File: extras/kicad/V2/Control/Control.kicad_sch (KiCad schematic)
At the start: 50 parts, among them J1 Ultrasonic Ranging, J2 Conn_01x05, J3 Output, J4 Input, J6 left, J7 right, P8 BeagleBone_Black_Header, P9 BeagleBone_Black_Header, U1 SparkFun-micromod, U2 ESP-01-WIFI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

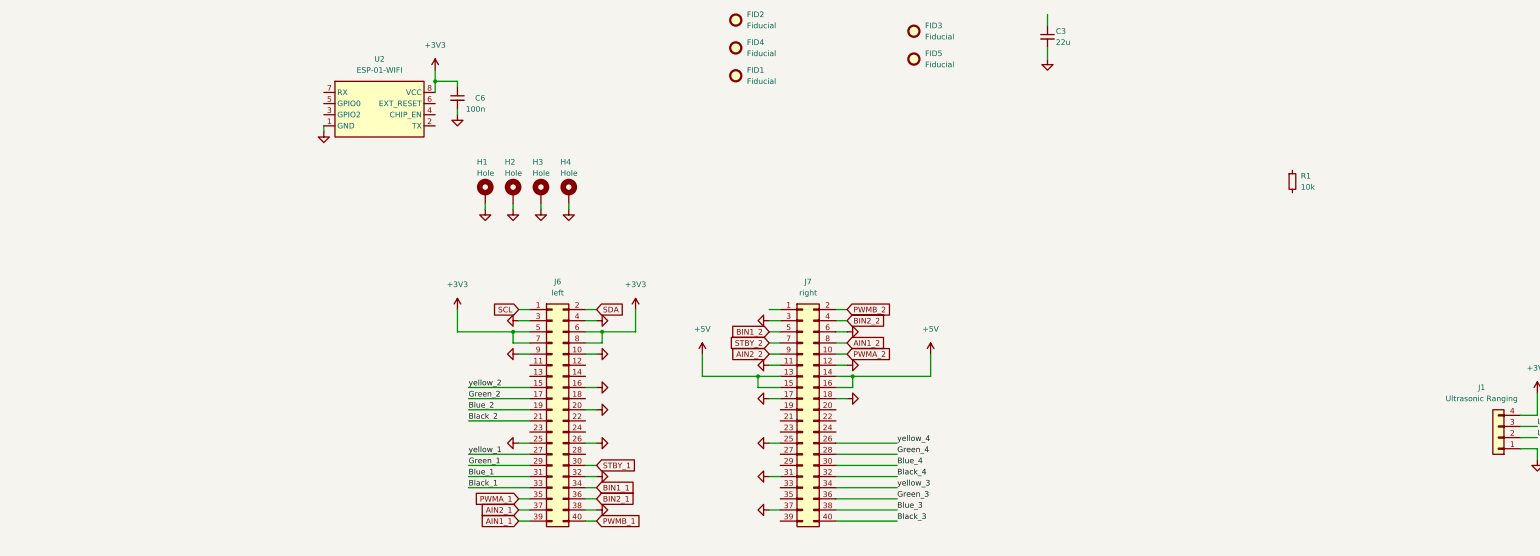
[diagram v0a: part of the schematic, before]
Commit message: Added UEXT, Mikroe & 7Pin SPI
(7pin SPI is break out garden) so we don't forget them
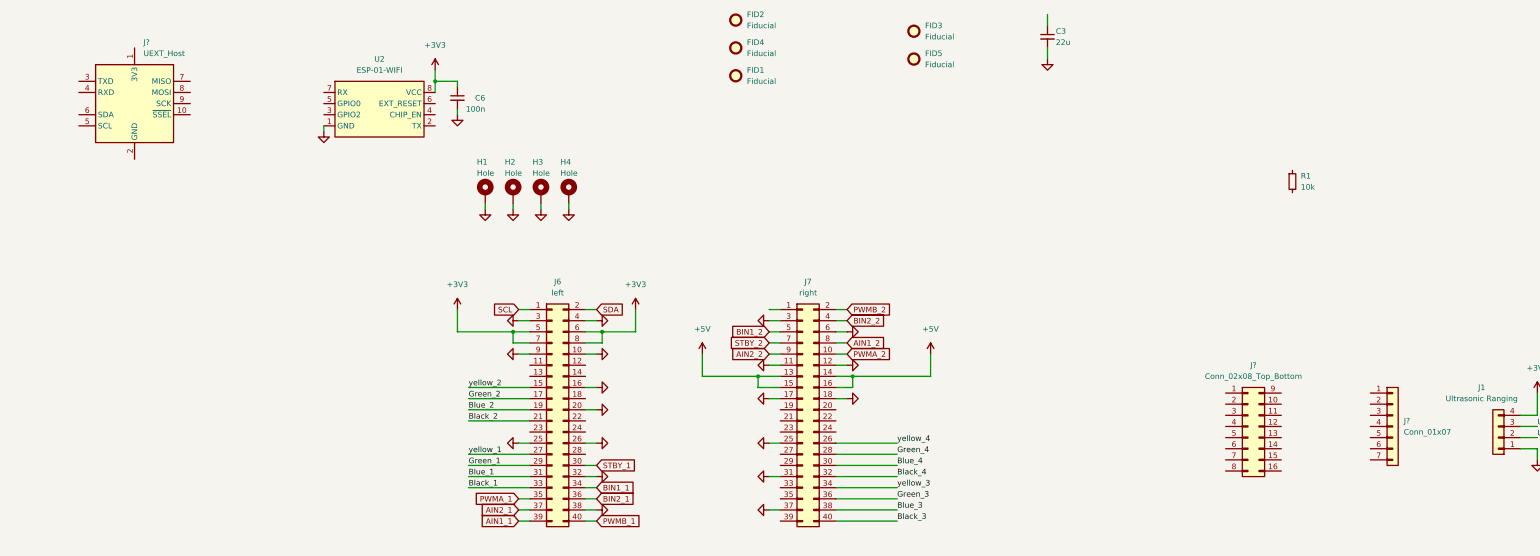
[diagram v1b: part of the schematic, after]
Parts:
- added J?: UEXT_Host, symbol Connector:UEXT_Host
- added J?: Conn_01x07, symbol Connector_Generic:Conn_01x07
- added J?: Conn_02x08_Top_Bottom, symbol Connector_Generic:Conn_02x08_Top_Bottom

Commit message: Added links to parts
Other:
- note added: "https://shop.pimoroni.com/products/spi-breakout-garden-extender-kit"
- note added: "https://www.mikroe.com/mikrobus-shuttle-127mm-2x8-pin-box-header-smd-male"
- note added: "https://www.olimex.com/Products/Modules/"
- moved on the sheet: J?
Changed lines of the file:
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@@
     (stroke (width 0) (type default) (color 0 0 0 0))
+  )
+  (text "https://shop.pimoroni.com/products/spi-breakout-garden-extender-kit"
+    (at 386.08 58.42 0)
+    (effects (font (size 1.27 1.27)) (justify left bottom))
   )
   (text "I2C ardress:\n001100X" (at 648.335 144.78 0)
@@
   )
   (text "0011[A2][A1][A0]" (at 536.575 146.685 0)
+    (effects (font (size 1.27 1.27)) (justify left bottom))
+  )
+  (text "https://www.mikroe.com/mikrobus-shuttle-127mm-2x8-pin-box-header-smd-male"
+    (at 368.3 35.56 0)
+    (effects (font (size 1.27 1.27)) (justify left bottom))
+  )
+  (text "https://www.olimex.com/Products/Modules/" (at 408.94 88.9 0)
     (effects (font (size 1.27 1.27)) (justify left bottom))
   )
@@
     (pin "1")
   )
-  (symbol (lib_id "Connector:UEXT_Host") (at 86.36 50.8 0) (unit 1)
-    (in_bom yes) (on_board yes) (fields_autoplaced)
-    (property "Reference" "J?" (id 0) (at 88.3794 36.83 0)
-      (effects (font (size 1.27 1.27)) (justify left))
-    )
-    (property "Value" "UEXT_Host" (id 1) (at 88.3794 39.37 0)
-      (effects (font (size 1.27 1.27)) (justify left))
-    )
-    (property "Footprint" "" (id 2) (at 82.55 50.8 0)
-      (effects (font (size 1.27 1.27)) hide)
-    )
-    (property "Datasheet" "https://www.olimex.com/Products/Modules/UEXT/resources/UEXT_rev_B.pdf" (id 3) (at 82.55 50.8 0)
+  (symbol (lib_id "Connector:UEXT_Host") (at 396.24 83.82 0) (unit 1)
+    (in_bom yes) (on_board yes) (fields_autoplaced)
+    (property "Reference" "J?" (id 0) (at 398.2594 69.85 0)
+      (effects (font (size 1.27 1.27)) (justify left))
+    )
+    (property "Value" "UEXT_Host" (id 1) (at 398.2594 72.39 0)
+      (effects (font (size 1.27 1.27)) (justify left))
+    )
+    (property "Footprint" "" (id 2) (at 392.43 83.82 0)
+      (effects (font (size 1.27 1.27)) hide)
+    )
+    (property "Datasheet" "https://www.olimex.com/Products/Modules/UEXT/resources/UEXT_rev_B.pdf" (id 3) (at 392.43 83.82 0)
       (effects (font (size 1.27 1.27)) hide)
     )
@@
     (pin "9")
   )
-  (symbol (lib_id "Connector_Generic:Conn_01x07") (at 373.38 124.46 0) (unit 1)
-    (in_bom yes) (on_board yes) (fields_autoplaced)
-    (property "Reference" "J?" (id 0) (at 375.92 123.1899 0)
-      (effects (font (size 1.27 1.27)) (justify left))
-    )
-    (property "Value" "Conn_01x07" (id 1) (at 375.92 125.7299 0)
-      (effects (font (size 1.27 1.27)) (justify left))
-    )
-    (property "Footprint" "" (id 2) (at 373.38 124.46 0)
-      (effects (font (size 1.27 1.27)) hide)
-    )
-    (property "Datasheet" "~" (id 3) (at 373.38 124.46 0)
+  (symbol (lib_id "Connector_Generic:Conn_01x07") (at 378.46 53.34 0) (unit 1)
+    (in_bom yes) (on_board yes) (fields_autoplaced)
+    (property "Reference" "J?" (id 0) (at 381 52.0699 0)
+      (effects (font (size 1.27 1.27)) (justify left))
+    )
+    (property "Value" "Conn_01x07" (id 1) (at 381 54.6099 0)
+      (effects (font (size 1.27 1.27)) (justify left))
+    )
+    (property "Footprint" "" (id 2) (at 378.46 53.34 0)
+      (effects (font (size 1.27 1.27)) hide)
+    )
+    (property "Datasheet" "~" (id 3) (at 378.46 53.34 0)
       (effects (font (size 1.27 1.27)) hide)
     )
@@
     (pin "1")
   )
-  (symbol (lib_id "Connector_Generic:Conn_02x08_Top_Bottom") (at 340.36 124.46 0) (unit 1)
-    (in_bom yes) (on_board yes) (fields_autoplaced)
-    (property "Reference" "J?" (id 0) (at 341.63 110.49 0))
-    (property "Value" "Conn_02x08_Top_Bottom" (id 1) (at 341.63 113.03 0))
-    (property "Footprint" "" (id 2) (at 340.36 124.46 0)
-      (effects (font (size 1.27 1.27)) hide)
-    )
-    (property "Datasheet" "~" (id 3) (at 340.36 124.46 0)
-      (effects (font (size 1.27 1.27)) hide)
-    )
+  (symbol (lib_id "Connector_Generic:Conn_02x08_Top_Bottom") (at 358.14 27.94 0) (unit 1)
+    (in_bom yes) (on_board yes) (fields_autoplaced)
+    (property "Reference" "J?" (id 0) (at 359.41 13.97 0))
+    (property "Value" "Conn_02x08_Top_Bottom" (id 1) (at 359.41 16.51 0))
+    (property "Footprint" "" (id 2) (at 358.14 27.94 0)
+      (effects (font (size 1.27 1.27)) hide)
+    )
+    (property "Datasheet" "~" (id 3) (at 358.14 27.94 0)
+      (effects (font (size 1.27 1.27)) hide)
+    )

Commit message: Update Control.kicad_sch
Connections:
- net +3V3: no longer U1.59 (SPI_COPI_(MOSI)), U1.61 (SPI_CIPO_(MISO)), U1.63 (G10), U1.65 (G9), U1.67 (G8), U1.69 (G7/BUS7), U1.71 (G6/BUS6), U1.73 (G5/BUS5)
- net BIN1_1: now also U1.66 (SDI_DATA1); no longer U1.51 (I2C_SDA1)
- net BIN2_1: now also U1.68 (SDI_DATA2); no longer U1.49 (BAT_VIN)
- net BIN2_2: now also U1.64 (SDI_DATA0); no longer U1.55 (SPI_CS)
- net CAN_STB: now also U1.38 (A1); no longer U1.47 (PWM1)
- net GND: now also U1.33 (GND)
- net Green_1: now also U1.10 (D0)
- net Green_2: now also U1.67 (G8)
- net Green_3: now also U1.63 (G10)
- net Green_4: now also U1.71 (G6/BUS6)
- net PWMA_2: now also U1.47 (PWM1); no longer U1.53 (I2C_SCL1)
- net PWMB_1: now also U1.32 (PWM0); no longer U1.58 (AUD_MCLK)
- net PWMB_2: now also U1.62 (SDI_CMD); no longer U1.57 (SPI_SCK)
- net yellow_1: now also U1.8 (G11)
- net yellow_2: now also U1.69 (G7/BUS7)
- net yellow_3: now also U1.65 (G9)
- net yellow_4: now also U1.73 (G5/BUS5)
- net ESP01_TX: now reaches U2.2 (TX)
- net ESP01_TX: now also U1.19 (UART_RX1)
- net ESP01_EN: now reaches U2.4 (CHIP_EN)
- net ESP01_EN: now also U1.15 (UART_CTS1)
- net ESP01_RST: now reaches U2.6 (EXT_RESET)
- net ESP01_RST: now also U1.13 (UART_RST1)
- net ESP01_RX: now reaches U2.7 (RX)
- net ESP01_RX: now also U1.17 (UART_TX1)
- net SWDCK: now reaches U1.21 (SWDCK)
- net SWDIO: now reaches U1.23 (SWDIO)
- new net CS1: U1.55 (SPI_CS)
- new net MISO: U1.61 (SPI_CIPO_(MISO))
- new net MOSI: U1.59 (SPI_COPI_(MOSI))
- new net SCK: U1.57 (SPI_SCK)
- no-connect marks 28 -> 33
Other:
- moved on the sheet: U2

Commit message: g
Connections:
- net AIN1_2: no longer U1.60 (SDI_SCK)
- net BIN1_1: no longer U1.66 (SDI_DATA1)
- net BIN2_1: no longer U1.68 (SDI_DATA2)
- net BIN2_2: no longer U1.64 (SDI_DATA0)
- net CAN_RX: no longer U1.41 (CAN_RX)
- net CAN_TX: no longer U1.43 (CAN_TX)
- net ESP01_EN: no longer U1.15 (UART_CTS1)
- net ESP01_RST: no longer U1.13 (UART_RST1)
- net Green_2: no longer U1.67 (G8)
- net Green_3: no longer U1.63 (G10)
- net PWMB_2: no longer U1.62 (SDI_CMD)
- net yellow_2: no longer U1.69 (G7/BUS7)
- net yellow_3: no longer U1.65 (G9)
- net SWDCK: no longer names the net of U1.21 (SWDCK)
- net SWDIO: no longer names the net of U1.23 (SWDIO)
- no-connect marks 33 -> 52

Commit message: Update Control.kicad_sch
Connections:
- net AIN1_1: now also U1.40 (G0/BUS0); no longer U1.48 (G4/BUS4)
- net AIN1_2: now also U1.48 (G4/BUS4)
- net AIN2_1: now also U1.42 (G1/BUS1); no longer U1.50 (AUD_BCLK)
- net AIN2_2: now also U1.44 (G2/BUS2); no longer U1.54 (AUD_IN)
- net BIN1_1: now also U1.34 (A0)
- net BIN1_2: now also U1.46 (G3/BUS3); no longer U1.56 (AUD_OUT)
- net BIN2_1: now also U1.38 (A1)
- net BIN2_2: now also U1.73 (G5/BUS5)
- net CAN_STB: no longer U1.38 (A1)
- net D2+: no longer U1.3 (USB_D+)
- net D2-: no longer U1.5 (USB_D-)
- net ESP01_RX: no longer U1.17 (UART_TX1)
- net ESP01_TX: no longer U1.19 (UART_RX1)
- net Green_1: no longer U1.10 (D0)
- net Green_4: no longer U1.71 (G6/BUS6)
- net INT: no longer U1.16 (I2C_INT)
- net INT_1: no longer U1.40 (G0/BUS0)
- net INT_2: no longer U1.42 (G1/BUS1)
- net PWMA_1: now also U1.10 (D0); no longer U1.52 (AUD_LRCLK)
- net PWMA_2: now also U1.18 (D1); no longer U1.47 (PWM1)
- net PWMB_2: now also U1.47 (PWM1)
- net Ultra_sound_Sig: no longer U1.46 (G3/BUS3)
- net Ultra_sound_Trig: no longer U1.44 (G2/BUS2)
- net yellow_1: no longer U1.8 (G11)
- net yellow_4: no longer U1.73 (G5/BUS5)
- net CS1 renamed SPI_CS
- net MISO renamed SPI_MOSI
- net MOSI renamed SPI_MISO
- net SCK renamed SPI_SCK
- no-connect marks 52 -> 51

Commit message: Update Control.kicad_sch
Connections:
- net I2C2.SCL is gone; now on net SCL: P9.19 (Pin_19)
- net I2C2.SDA is gone; now on net SDA: P9.20 (Pin_20)
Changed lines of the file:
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@@
     (stroke (width 0) (type solid) (color 0 0 0 0))
   )
-  (wire (pts (xy 55.88 250.19) (xy 63.5 250.19))
+  (wire (pts (xy 58.42 250.19) (xy 63.5 250.19))
     (stroke (width 0) (type default) (color 0 0 0 0))
   )
@@
     (stroke (width 0) (type solid) (color 0 0 0 0))
   )
+  (wire (pts (xy 172.72 261.62) (xy 183.515 261.62))
+    (stroke (width 0) (type default) (color 0 0 0 0))
+  )
   (wire (pts (xy 461.01 453.39) (xy 468.63 453.39))
     (stroke (width 0) (type default) (color 0 0 0 0))
@@
     (stroke (width 0) (type default) (color 0 0 0 0))
   )
-  (wire (pts (xy 55.88 247.65) (xy 63.5 247.65))
+  (wire (pts (xy 58.42 247.65) (xy 63.5 247.65))
     (stroke (width 0) (type default) (color 0 0 0 0))
   )
@@
   )
   (wire (pts (xy 466.09 466.09) (xy 468.63 466.09))
+    (stroke (width 0) (type default) (color 0 0 0 0))
+  )
+  (wire (pts (xy 172.72 259.08) (xy 183.515 259.08))
     (stroke (width 0) (type default) (color 0 0 0 0))
   )
@@
     (effects (font (size 1.27 1.27)) (justify right bottom))
   )
+  (label "yellow_1" (at 153.035 227.33 0)
+    (effects (font (size 1.27 1.27)) (justify left bottom))
+  )
   (label "yellow_2" (at 162.56 115.57 0)
     (effects (font (size 1.27 1.27)) (justify left bottom))
@@
     (effects (font (size 1.27 1.27)) (justify right bottom))
   )
+  (label "Green_2" (at 153.035 215.265 0)
+    (effects (font (size 1.27 1.27)) (justify left bottom))
+  )
   (label "Blue_1" (at 774.7 71.12 0)
     (effects (font (size 1.27 1.27)) (justify left bottom))
@@
     (effects (font (size 1.27 1.27)) (justify right bottom))
   )
+  (label "I2C2.SDA" (at 183.515 261.62 180)
+    (effects (font (size 1.27 1.27)) (justify right bottom))
+  )
+  (label "yellow_2" (at 153.035 212.725 0)
+    (effects (font (size 1.27 1.27)) (justify left bottom))
+  )
   (label "Blue_3" (at 260.35 143.51 0)
     (effects (font (size 1.27 1.27)) (justify left bottom))
   )
+  (label "yellow_3" (at 153.035 222.25 0)
+    (effects (font (size 1.27 1.27)) (justify left bottom))
+  )
   (label "GPIO[117]" (at 198.12 262.89 0)
     (effects (font (size 1.27 1.27)) (justify left bottom))
@@
     (effects (font (size 1.27 1.27)) (justify right bottom))
   )
+  (label "Green_1" (at 153.035 229.87 0)
+    (effects (font (size 1.27 1.27)) (justify left bottom))
+  )
   (label "GPIO[69]" (at 261.62 242.57 0)
     (effects (font (size 1.27 1.27)) (justify left bottom))
@@
     (effects (font (size 1.27 1.27)) (justify left bottom))
   )
+  (label "Green_3" (at 153.035 224.79 0)
+    (effects (font (size 1.27 1.27)) (justify left bottom))
+  )
   (label "GPIO[46]" (at 312.42 250.19 180)
     (effects (font (size 1.27 1.27)) (justify right bottom))
@@
     (effects (font (size 1.27 1.27)) (justify right bottom))
   )
+  (label "yellow_4" (at 153.035 217.17 0)
+    (effects (font (size 1.27 1.27)) (justify left bottom))
+  )
   (label "MMC1.DAT[3]" (at 312.42 237.49 180)
     (effects (font (size 1.27 1.27)) (justify right bottom))
@@
     (effects (font (size 1.27 1.27)) (justify right bottom))
   )
+  (label "I2C2.SCL" (at 183.515 259.08 180)
+    (effects (font (size 1.27 1.27)) (justify right bottom))
+  )
   (label "LCD.DATA[9]" (at 312.42 278.13 180)
     (effects (font (size 1.27 1.27)) (justify right bottom))
@@
   )
   (label "LCD.DATA[2]" (at 261.62 283.21 0)
+    (effects (font (size 1.27 1.27)) (justify left bottom))
+  )
+  (label "Green_4" (at 153.035 219.71 0)
     (effects (font (size 1.27 1.27)) (justify left bottom))
   )
@@
     )
   )
-  (global_label "BIN1_1" (shape input) (at 55.88 247.65 180) (fields_autoplaced)
-    (effects (font (size 1.27 1.27)) (justify right))
-    (property "Intersheet References" "${INTERSHEET_REFS}" (id 0) (at 46.875 247.7294 0)
+  (global_label "BIN1_1" (shape input) (at 58.42 247.65 180) (fields_autoplaced)
+    (effects (font (size 1.27 1.27)) (justify right))
+    (property "Intersheet References" "${INTERSHEET_REFS}" (id 0) (at 49.415 247.7294 0)
       (effects (font (size 1.27 1.27)) (justify right) hide)
     )
@@
     )
   )
+  (global_label "SCL" (shape input) (at 172.72 259.08 180) (fields_autoplaced)
+    (effects (font (size 1.27 1.27)) (justify right))
+    (property "Intersheet References" "${INTERSHEET_REFS}" (id 0) (at 166.7993 259.0006 0)
+      (effects (font (size 1.27 1.27)) (justify right) hide)
+    )
+  )
   (global_label "SDA" (shape input) (at 542.29 124.46 180) (fields_autoplaced)
     (effects (font (size 1.27 1.27)) (justify right))
@@
     )
   )
+  (global_label "SDA" (shape input) (at 172.72 261.62 180) (fields_autoplaced)
+    (effects (font (size 1.27 1.27)) (justify right))
+    (property "Intersheet References" "${INTERSHEET_REFS}" (id 0) (at 166.7388 261.5406 0)
+      (effects (font (size 1.27 1.27)) (justify right) hide)
+    )
+  )
   (global_label "BIN2_2" (shape input) (at 107.95 196.85 0) (fields_autoplaced)
     (effects (font (size 1.27 1.27)) (justify left))
@@
     )
   )
-  (global_label "PWMB_1" (shape input) (at 55.88 250.19 180) (fields_autoplaced)
-    (effects (font (size 1.27 1.27)) (justify right))
-    (property "Intersheet References" "${INTERSHEET_REFS}" (id 0) (at 45.8469 250.1106 0)
-      (effects (font (size 1.27 1.27)) (justify right) hide)
-    )
+  (global_label "PWMB_1" (shape input) (at 58.42 250.19 180) (fields_autoplaced)
+    (effects (font (size 1.27 1.27)) (justify right))
+    (property "Intersheet References" "${INTERSHEET_REFS}" (id 0) (at 48.3869 250.1106 0)
+      (effects (font (size 1.27 1.27)) (justify right) hide)
+    )

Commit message: h
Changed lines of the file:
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@@
     (effects (font (size 1.27 1.27)) (justify right bottom))
   )
-  (label "yellow_1" (at 153.035 227.33 0)
+  (label "yellow_1" (at 146.05 226.695 0)
     (effects (font (size 1.27 1.27)) (justify left bottom))
   )
@@
     (effects (font (size 1.27 1.27)) (justify right bottom))
   )
-  (label "Green_2" (at 153.035 215.265 0)
+  (label "Green_2" (at 146.05 214.63 0)
     (effects (font (size 1.27 1.27)) (justify left bottom))
   )
@@
     (effects (font (size 1.27 1.27)) (justify right bottom))
   )
-  (label "yellow_2" (at 153.035 212.725 0)
+  (label "yellow_2" (at 146.05 212.09 0)
     (effects (font (size 1.27 1.27)) (justify left bottom))
   )
@@
     (effects (font (size 1.27 1.27)) (justify left bottom))
   )
-  (label "yellow_3" (at 153.035 222.25 0)
+  (label "yellow_3" (at 146.05 221.615 0)
     (effects (font (size 1.27 1.27)) (justify left bottom))
   )
@@
     (effects (font (size 1.27 1.27)) (justify right bottom))
   )
-  (label "Green_1" (at 153.035 229.87 0)
+  (label "Green_1" (at 146.05 229.235 0)
     (effects (font (size 1.27 1.27)) (justify left bottom))
   )
@@
     (effects (font (size 1.27 1.27)) (justify left bottom))
   )
-  (label "Green_3" (at 153.035 224.79 0)
+  (label "Green_3" (at 146.05 224.155 0)
     (effects (font (size 1.27 1.27)) (justify left bottom))
   )
@@
     (effects (font (size 1.27 1.27)) (justify right bottom))
   )
-  (label "yellow_4" (at 153.035 217.17 0)
+  (label "yellow_4" (at 146.05 216.535 0)
     (effects (font (size 1.27 1.27)) (justify left bottom))
   )
@@
     (effects (font (size 1.27 1.27)) (justify left bottom))
   )
-  (label "Green_4" (at 153.035 219.71 0)
-    (effects (font (size 1.27 1.27)) (justify left bottom))
-  )
+  (label "Green_4" (at 146.05 219.075 0)
+    (effects (font (size 1.27 1.27)) (justify left bottom))
+  )

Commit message: Minor schematic change
t
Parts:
- removed C6: 100n, Capacitor_SMD:C_0603_1608Metric_Pad1.08x0.95mm_HandSolder, symbol Device:C_Small
- removed J?: Conn_01x07, symbol Connector_Generic:Conn_01x07
- removed U2: ESP-01-WIFI, Connector_PinHeader_2.54mm:PinHeader_2x04_P2.54mm_Vertical, symbol My_custom_lib:ESP-01-WIFI
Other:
- note removed: "https://shop.pimoroni.com/products/spi-breakout-garden-extender-kit"
- moved on the sheet: J?
